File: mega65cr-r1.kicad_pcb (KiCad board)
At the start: 4 copper layers, 435 x 140 mm, 184 parts, among them J1 DB9_Male_MountingHoles, J10 Molex 46765-2301, J11 CON-SOCJ-2155, J12 Header for power lead to QMTE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, J13 Conn_01x04_Male, J14 Conn_02x17_Odd_Even, J15 696101000002 Fuse Holder 20mm, J16 Conn_01x04_Male, J17 C64_Tape_Port, J18 BA60BC0WT, J19 C64_User_Port, J2 DB9_Male_MountingHoles, J20 C64_Expansion_Port, J21 Audio Header, J22 DB15_Female_HighDensity_Mount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, J23 3.5mm_Stereo_Audio_Jack STX-3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, J24 Component A/V, J25 Joystick Ports Mezannine Lower, J26 Joystick Ports Mezannine Upper, J3 Wuerth_7499010121A, J4 QMTECH FPGA Module U4, J5 QMTECH FPGA Module U5, J6 SDF-60J for IEC 1541 serial p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, J7 QMTECH JTAG, J8 RTC, J9 1140084168 microSD Card Slot, P1 Full-side CD Card Slot, SW1 SW_Push_DPDT, U1 74LS373, U10 74LS06N, U11 74LS06N, U12 DP83826, U13 74LVC374, U14 PTN3363BSMP, U15 LM2678T-5.0, U16 74LVC374, U17 74LVC374, U18 74LS373, U19 74LS373, U2 74LVC374, U20 74LS125, U21 74LS125, U22 74LS06N, U23 74LVC374, U24 74LS125, U25 74LS373, U26 74LS373, U27 74LS138, U28 74LS138, U29 74LS137, U3 74LVC374, U30 74LS137, U31 74LS04, U32 74LVC374, U33 74LVC374, U34 74LVC374, U35 74LS373, U36 74LS373, U37 74LS373, U38 74LVC374, U39 74LVC374, U4 74LS373, U40 74LS373, U41 74LS373, U5 74LS06N, U6 74LVC374, U7 74LVC374, U8 74LS373, U9 74LS373

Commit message: replace remaining 74LS373 with 74LS374s #5
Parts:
- U1 (x2), U18, U19, U25, U26, U35, U36, U37, U4 (x2), U40, U41, U8, U9: value 74LS373 -> 74LS374

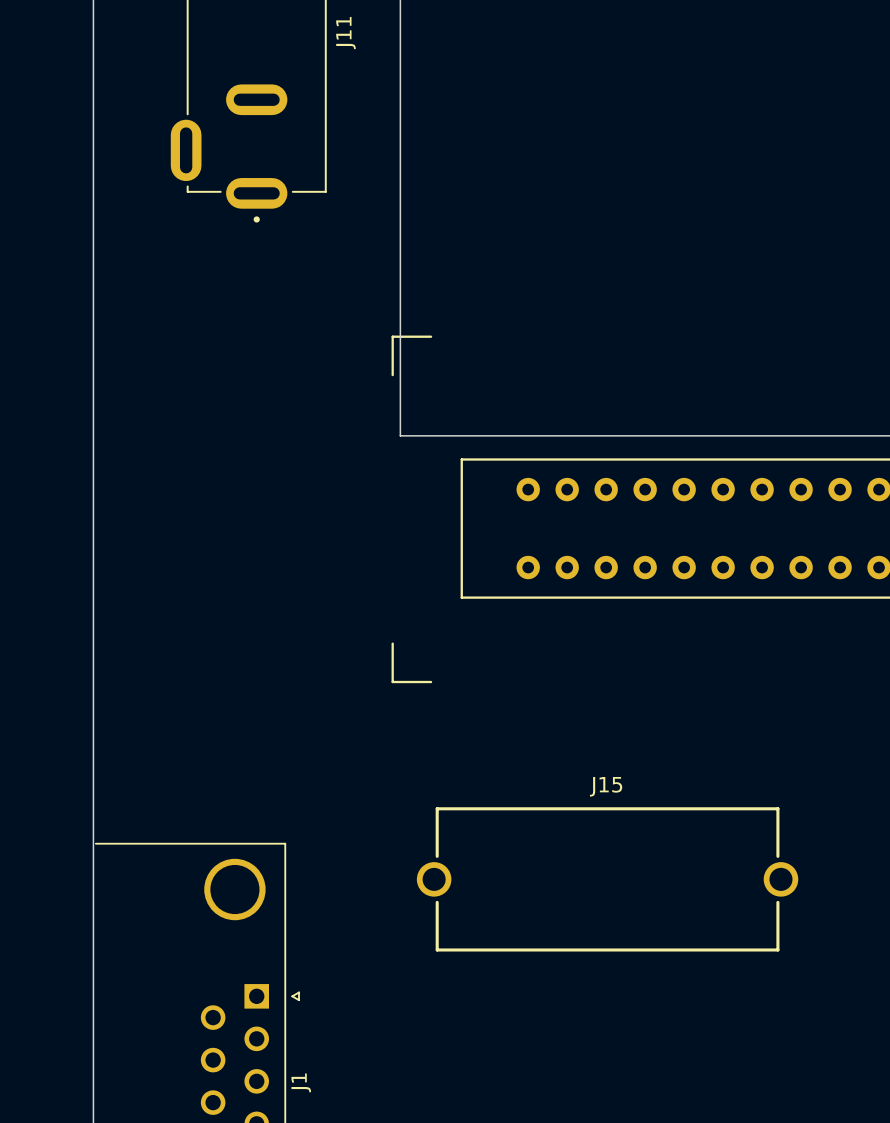
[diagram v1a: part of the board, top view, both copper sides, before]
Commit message: add missing power switch #7
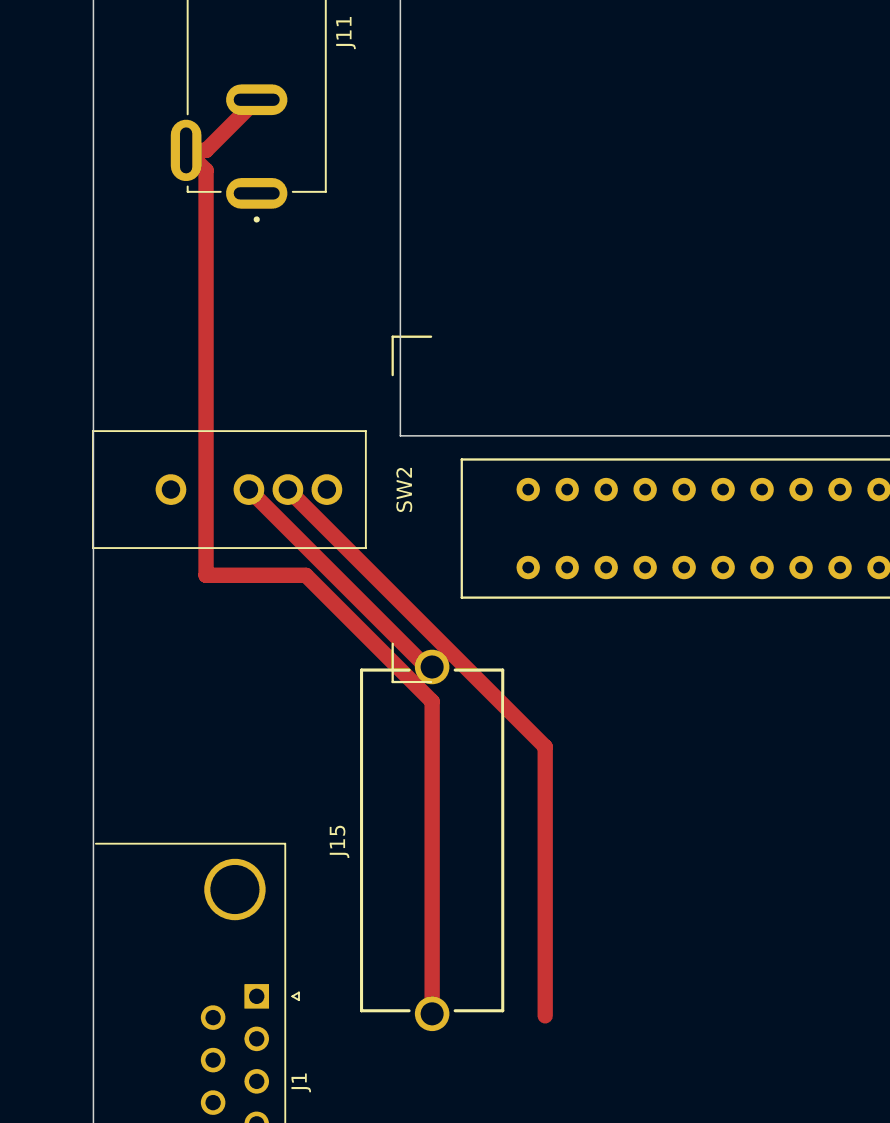
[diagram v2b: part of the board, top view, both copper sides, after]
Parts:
- added SW2: SW_SPDT_with_shield, snapeda:T103J1AVBE2, F.Cu at (50.3, 62.2)
- U1 (x2), U4 (x2), U9: value 74LS374 -> 74LS373
- moved J15 11.7 mm to (52.1, 86.4), turned to 90 degrees
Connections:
- J11 pad 2: /Power Supply/VBAT -> +12V_FUSED
- J11 pad 3: /Power Supply/VBAT -> +12V_FUSED
- J15 pad 1: /Power Supply/VBAT -> +12V_FUSED
- RN4 pad 4: /Cartridge Port/PHI2 -> unconnected-(RN4-Pad4)
- RN4 pad 5: /Cartridge Port/NMI_N -> /Cartridge Port/DMA_N
- RN4 pad 6: /Cartridge Port/RESET_N -> /Cartridge Port/R_W
- RN4 pad 7: /Cartridge Port/ROMH_N -> /Cartridge Port/NMI_N
- RN4 pad 8: /Cartridge Port/DMA_N -> /Cartridge Port/IRQ_N
- RN4 pad 9: /Cartridge Port/BA -> /Cartridge Port/RESET_N
- U32 pad 13: /Cartridge Port/NMI_N -> /Cartridge Port/DMA_N
- U32 pad 14: /Cartridge Port/PHI2 -> /Cartridge Port/ROML_N
- U32 pad 17: unconnected-(U32-Pad17) -> /Cartridge Port/ROMH_N
- U32 pad 18: unconnected-(U32-Pad18) -> /Cartridge Port/BA
- U32 pad 3: /Cartridge Port/BA -> /Cartridge Port/RESET_N
- U32 pad 4: /Cartridge Port/DMA_N -> /Cartridge Port/IRQ_N
- U32 pad 7: /Cartridge Port/ROMH_N -> /Cartridge Port/NMI_N
- U32 pad 8: /Cartridge Port/RESET_N -> /Cartridge Port/R_W
- U35 pad 12: /Cartridge Port/NMI_N -> /Cartridge Port/DMA_P_DRIVE
- U35 pad 15: /Cartridge Port/PHI2 -> /Cartridge Port/ROML_N
- U35 pad 16: unconnected-(U35-Pad16) -> /Cartridge Port/ROMH_N
- U35 pad 19: unconnected-(U35-Pad19) -> /Cartridge Port/BA
- U35 pad 2: /Cartridge Port/BA -> /Cartridge Port/RESET_P_DRIVE
- U35 pad 5: /Cartridge Port/DMA_N -> /Cartridge Port/IRQ_P_DRIVE
- U35 pad 6: /Cartridge Port/ROMH_N -> /Cartridge Port/NMI_P_DRIVE
- U35 pad 9: /Cartridge Port/RESET_N -> /Cartridge Port/W_R_DRIVE
- U38 pad 18: /Cartridge Port/ROML_N -> /Cartridge Port/PHI2
- U38 pad 3: /Cartridge Port/IRQ_N -> unconnected-(U38-Pad3)
- U38 pad 4: /Cartridge Port/R_W -> unconnected-(U38-Pad4)
- U40 pad 19: /Cartridge Port/ROML_N -> /Cartridge Port/PHI2
- U40 pad 2: /Cartridge Port/IRQ_N -> unconnected-(U40-Pad2)
- U40 pad 5: /Cartridge Port/R_W -> unconnected-(U40-Pad5)
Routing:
- net +12V_FUSED: track 0.00 -> 130.6 mm

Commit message: correct position of power input and switch and cart port
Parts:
- moved J11 3.44 mm to (37.2, 38.1)
- moved SW2 1.53 mm to (50.3, 63.8)
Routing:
- net +12V_FUSED: track 130.6 -> 132.1 mm
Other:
- outline, holes or cut-outs redrawn
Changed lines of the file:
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@@
   )
   (footprint "snapeda:GRAVITECH_CON-SOCJ-2155" (layer "F.Cu")
-    (at 40.64 38.1 -90)
+    (at 37.2 38.1 -90)
     (property "MANUFACTURER" "Gravitech")
     (property "MAXIMUM_PACKAGE_HEIGHT" "11.1 mm")
@@
   )
   (footprint "snapeda:T103J1AVBE2" (layer "F.Cu")
-    (at 50.292 62.23 90)
+    (at 50.292 63.76 90)
     (property "Sheetfile" "power.kicad_sch")
     (property "Sheetname" "Power Supply")
@@
   (gr_line (start 417.5 118.5) (end 439 140) (layer "Edge.Cuts") (width 0.1))
   (gr_line (start 360 65) (end 465 65) (layer "Edge.Cuts") (width 0.1))
-  (gr_line (start 120 30) (end 465 30) (layer "Edge.Cuts") (width 0.1))
+  (gr_line (start 121 30) (end 465 30) (layer "Edge.Cuts") (width 0.1))
   (gr_line (start 50 30) (end 50 60) (layer "Edge.Cuts") (width 0.1))
+  (gr_line (start 115 50) (end 115 60) (layer "Edge.Cuts") (width 0.1))
   (gr_line (start 360 170) (end 30 170) (layer "Edge.Cuts") (width 0.1))
   (gr_line (start 30 170) (end 30 30) (layer "Edge.Cuts") (width 0.1))
   (gr_line (start 360 170) (end 360 65) (layer "Edge.Cuts") (width 0.1))
   (gr_line (start 30 30) (end 50 30) (layer "Edge.Cuts") (width 0.1))
-  (gr_line (start 120 60) (end 120 30) (layer "Edge.Cuts") (width 0.1))
+  (gr_line (start 121 60) (end 115 60) (layer "Edge.Cuts") (width 0.1))
+  (gr_line (start 121 60) (end 121 30) (layer "Edge.Cuts") (width 0.1))
+  (gr_line (start 56 60) (end 56 50) (layer "Edge.Cuts") (width 0.1))
   (gr_line (start 465 30) (end 465 65) (layer "Edge.Cuts") (width 0.1))
   (gr_line (start 465 140) (end 465 65) (layer "Edge.Cuts") (width 0.1))
-  (gr_line (start 50 60) (end 120 60) (layer "Edge.Cuts") (width 0.1))
+  (gr_line (start 50 60) (end 56 60) (layer "Edge.Cuts") (width 0.1))
+  (gr_line (start 56 50) (end 115 50) (layer "Edge.Cuts") (width 0.1))
   (gr_text "MEGA65CR R1\nJoystick Port\nMezzannine" (at 439.367 126.716 270) (layer "F.SilkS")
     (effects (font (size 1 1) (thickness 0.15)) (justify left))
@@
   (segment (start 457.147 89.891) (end 457.65 89.891) (width 0.25) (layer "B.Cu") (net 2))
   (segment (start 453.347 80.991) (end 453.85 80.991) (width 0.25) (layer "B.Cu") (net 2))
-  (segment (start 37.338 42.698) (end 36.04 41.4) (width 1) (layer "F.Cu") (net 3))
+  (segment (start 37.338 69.088) (end 37.338 51.562) (width 1) (layer "F.Cu") (net 3))
+  (segment (start 52.07 97.66) (end 52.07 77.311143) (width 1) (layer "F.Cu") (net 3))
   (segment (start 59.436 80.264) (end 59.436 97.79) (width 1) (layer "F.Cu") (net 3))
-  (segment (start 37.338 69.088) (end 37.338 42.698) (width 1) (layer "F.Cu") (net 3))
-  (segment (start 36.04 41.4) (end 37.34 41.4) (width 1) (layer "F.Cu") (net 3))
+  (segment (start 37.338 51.562) (end 32.6 46.824) (width 1) (layer "F.Cu") (net 3))
   (segment (start 43.846857 69.088) (end 37.338 69.088) (width 1) (layer "F.Cu") (net 3))
+  (segment (start 32.6 41.4) (end 33.9 41.4) (width 1) (layer "F.Cu") (net 3))
   (segment (start 40.132 63.5) (end 51.692 75.06) (width 1) (layer "F.Cu") (net 3))
+  (segment (start 33.9 41.4) (end 37.2 38.1) (width 1) (layer "F.Cu") (net 3))
+  (segment (start 32.6 46.824) (end 32.6 41.4) (width 1) (layer "F.Cu") (net 3))
   (segment (start 42.672 63.5) (end 59.436 80.264) (width 1) (layer "F.Cu") (net 3))
-  (segment (start 52.07 97.66) (end 52.07 77.311143) (width 1) (layer "F.Cu") (net 3))
   (segment (start 52.07 77.311143) (end 43.846857 69.088) (width 1) (layer "F.Cu") (net 3))
-  (segment (start 37.34 41.4) (end 40.64 38.1) (width 1) (layer "F.Cu") (net 3))
   (segment (start 51.692 75.06) (end 52.07 75.06) (width 0.25) (layer "B.Cu") (net 3))
   (segment (start 457.782 85.446) (end 457.782 82.774) (width 0.25) (layer "B.Cu") (net 6))

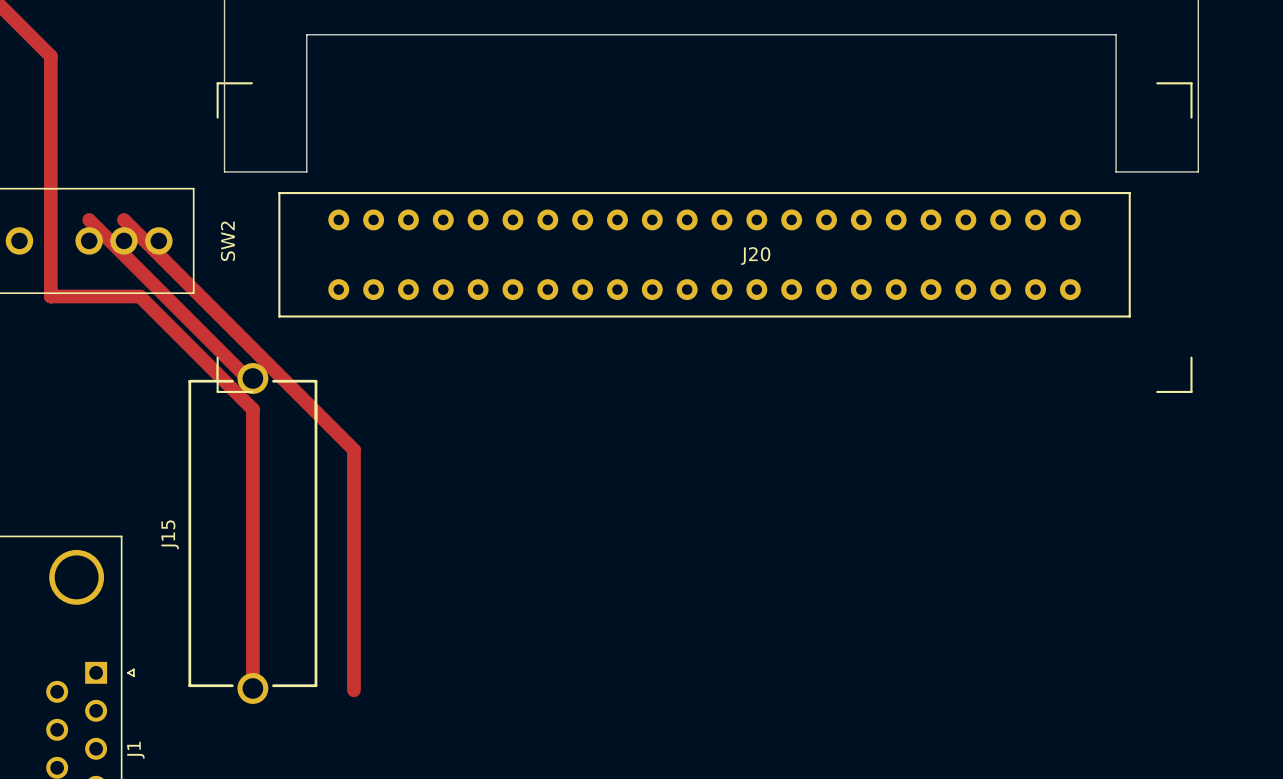
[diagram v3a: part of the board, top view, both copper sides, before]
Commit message: further fix cart port and power switch connections #2
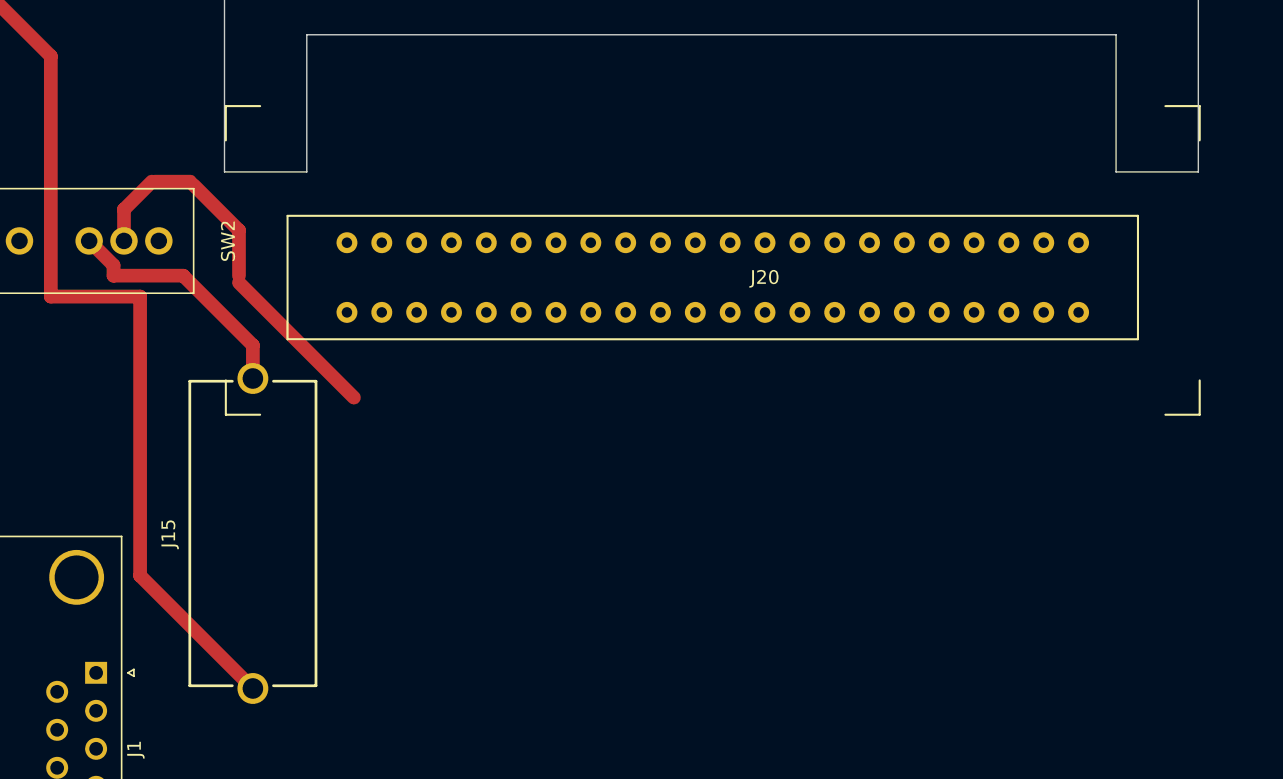
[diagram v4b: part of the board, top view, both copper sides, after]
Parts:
- moved J20 1.76 mm to (85.6, 67.7)
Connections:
- J11 pad 2: +12V_FUSED -> Net-(SW2-Pad3)
- J11 pad 3: +12V_FUSED -> Net-(SW2-Pad3)
- J15 pad 1: +12V_FUSED -> Net-(SW2-Pad3)
- J15 pad 2: +12V_FUSED -> Net-(SW2-Pad3)
- SW2 pad 3: +12V_FUSED -> Net-(SW2-Pad3)
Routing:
- net +12V_FUSED: track 132.1 -> 28.7 mm
- net Net-(SW2-Pad3): track 0.00 -> 92.4 mm
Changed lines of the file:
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@@
   (net 502 "unconnected-(U40-Pad5)")
   (net 503 "unconnected-(SW2-Pad1)")
+  (net 504 "Net-(SW2-Pad3)")
   (footprint "Resistor_THT:R_Axial_DIN0204_L3.6mm_D1.6mm_P7.62mm_Horizontal" (layer "F.Cu")
     (at 183.61 287.04)
@@
       (net 180 "unconnected-(J11-Pad1)") (pintype "passive"))
     (pad "2" thru_hole oval locked (at 3.3 4.6 270) (size 4 2) (drill oval 3 0.8) (layers *.Cu *.Mask)
-      (net 3 "+12V_FUSED") (pintype "passive"))
+      (net 504 "Net-(SW2-Pad3)") (pintype "passive"))
     (pad "3" thru_hole oval locked (at 0 0 270) (size 2 4) (drill oval 0.8 3) (layers *.Cu *.Mask)
-      (net 3 "+12V_FUSED") (pintype "passive"))
+      (net 504 "Net-(SW2-Pad3)") (pintype "passive"))
   )
   (footprint "Resistor_THT:R_Box_L8.4mm_W2.5mm_P5.08mm" (layer "F.Cu")
@@
   )
   (footprint "HackupNet:C64-Cart-Socket-Vertical" (layer "F.Cu")
-    (at 85 66.04)
+    (at 85.598 67.7)
     (property "Sheetfile" "expansionport.kicad_sch")
     (property "Sheetname" "Cartridge Port")
@@
     (fp_line (start 11 -4.5) (end 11 4.5) (layer "F.Fab") (width 0.1))
     (pad "1" thru_hole circle locked (at -11.3 0 90) (size 2.25 2.25) (drill 1.5) (layers *.Cu *.Mask)
-      (net 3 "+12V_FUSED") (pintype "passive"))
+      (net 504 "Net-(SW2-Pad3)") (pintype "passive"))
     (pad "2" thru_hole circle locked (at 11.3 0 90) (size 2.25 2.25) (drill 1.5) (layers *.Cu *.Mask)
-      (net 3 "+12V_FUSED") (pintype "passive"))
+      (net 504 "Net-(SW2-Pad3)") (pintype "passive"))
   )
   (footprint "Package_DIP:DIP-20_W7.62mm" (layer "F.Cu")
@@
       (net 3 "+12V_FUSED") (pinfunction "B") (pintype "passive"))
     (pad "3" thru_hole circle (at -1.27 -10.16 90) (size 2 2) (drill 1.2) (layers *.Cu *.Mask)
-      (net 3 "+12V_FUSED") (pinfunction "C") (pintype "passive"))
+      (net 504 "Net-(SW2-Pad3)") (pinfunction "C") (pintype "passive"))
     (pad "SH" thru_hole circle (at -1.27 -15.24 90) (size 2 2) (drill 1.2) (layers *.Cu *.Mask)
       (net 2 "GND") (pinfunction "SHIELD") (pintype "passive"))
@@
   (segment (start 457.147 89.891) (end 457.65 89.891) (width 0.25) (layer "B.Cu") (net 2))
   (segment (start 453.347 80.991) (end 453.85 80.991) (width 0.25) (layer "B.Cu") (net 2))
-  (segment (start 37.338 69.088) (end 37.338 51.562) (width 1) (layer "F.Cu") (net 3))
-  (segment (start 52.07 97.66) (end 52.07 77.311143) (width 1) (layer "F.Cu") (net 3))
-  (segment (start 59.436 80.264) (end 59.436 97.79) (width 1) (layer "F.Cu") (net 3))
-  (segment (start 37.338 51.562) (end 32.6 46.824) (width 1) (layer "F.Cu") (net 3))
-  (segment (start 43.846857 69.088) (end 37.338 69.088) (width 1) (layer "F.Cu") (net 3))
-  (segment (start 32.6 41.4) (end 33.9 41.4) (width 1) (layer "F.Cu") (net 3))
-  (segment (start 40.132 63.5) (end 51.692 75.06) (width 1) (layer "F.Cu") (net 3))
-  (segment (start 33.9 41.4) (end 37.2 38.1) (width 1) (layer "F.Cu") (net 3))
-  (segment (start 32.6 46.824) (end 32.6 41.4) (width 1) (layer "F.Cu") (net 3))
-  (segment (start 42.672 63.5) (end 59.436 80.264) (width 1) (layer "F.Cu") (net 3))
-  (segment (start 52.07 77.311143) (end 43.846857 69.088) (width 1) (layer "F.Cu") (net 3))
-  (segment (start 51.692 75.06) (end 52.07 75.06) (width 0.25) (layer "B.Cu") (net 3))
+  (segment (start 42.672 62.738) (end 44.704 60.706) (width 1) (layer "F.Cu") (net 3))
+  (segment (start 51.054 64.262) (end 51.054 67.564) (width 1) (layer "F.Cu") (net 3))
+  (segment (start 51.054 68.072) (end 59.436 76.454) (width 1) (layer "F.Cu") (net 3))
+  (segment (start 51.054 67.564) (end 51.054 68.072) (width 0.25) (layer "F.Cu") (net 3))
+  (segment (start 42.672 65.03) (end 42.672 62.738) (width 1) (layer "F.Cu") (net 3))
+  (segment (start 44.958 60.706) (end 47.498 60.706) (width 1) (layer "F.Cu") (net 3))
+  (segment (start 47.752 60.96) (end 51.054 64.262) (width 1) (layer "F.Cu") (net 3))
+  (segment (start 47.498 60.706) (end 47.752 60.96) (width 0.25) (layer "F.Cu") (net 3))
+  (segment (start 44.704 60.706) (end 44.958 60.706) (width 0.25) (layer "F.Cu") (net 3))
   (segment (start 457.782 85.446) (end 457.782 82.774) (width 0.25) (layer "B.Cu") (net 6))
   (segment (start 442.851031 67.351969) (end 442.851031 66.716969) (width 0.25) (layer "B.Cu") (net 6))
@@
   (segment (start 440.368794 136.735511) (end 423.364641 119.731359) (width 0.25) (layer "B.Cu") (net 491))
   (segment (start 449.50565 136.34665) (end 449.116789 136.735511) (width 0.25) (layer "B.Cu") (net 491))
+  (segment (start 37.338 69.088) (end 37.338 51.562) (width 1) (layer "F.Cu") (net 504))
+  (segment (start 43.846857 69.088) (end 43.846857 89.436857) (width 1) (layer "F.Cu") (net 504))
+  (segment (start 41.91 67.564) (end 46.99 67.564) (width 1) (layer "F.Cu") (net 504))
+  (segment (start 37.338 51.562) (end 32.6 46.824) (width 1) (layer "F.Cu") (net 504))
+  (segment (start 43.846857 69.088) (end 37.338 69.088) (width 1) (layer "F.Cu") (net 504))
+  (segment (start 32.6 41.4) (end 33.9 41.4) (width 1) (layer "F.Cu") (net 504))
+  (segment (start 33.9 41.4) (end 37.2 38.1) (width 1) (layer "F.Cu") (net 504))
+  (segment (start 41.91 66.808) (end 41.91 67.564) (width 1) (layer "F.Cu") (net 504))
+  (segment (start 52.07 72.644) (end 52.07 75.06) (width 1) (layer "F.Cu") (net 504))
+  (segment (start 32.6 46.824) (end 32.6 41.4) (width 1) (layer "F.Cu") (net 504))
+  (segment (start 46.99 67.564) (end 52.07 72.644) (width 1) (layer "F.Cu") (net 504))
+  (segment (start 40.132 65.03) (end 41.91 66.808) (width 1) (layer "F.Cu") (net 504))
+  (segment (start 43.846857 89.436857) (end 52.07 97.66) (width 1) (layer "F.Cu") (net 504))
+  (segment (start 51.692 75.06) (end 52.07 75.06) (width 0.25) (layer "B.Cu") (net 504))
   (zone (net 2) (net_name "GND") (layers "In1.Cu" "In2.Cu") (hatch edge 0.508)
     (connect_pads (clearance 0.508))

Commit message: correct port positions and cutouts #2
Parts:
- moved J23 11.5 mm to (240.0, 38.1)
- moved J9 10.3 mm to (226.0, 41.0)
- moved J10 8.94 mm to (189.0, 41.0)
- moved J22 8.63 mm to (157.0, 43.0)
- moved U14 7.48 mm to (193.4, 53.2)
- moved J24 6.56 mm to (352.0, 38.1)
- moved J3 5.95 mm to (205.5, 45.6)
- moved J17 4.53 mm to (442.0, 41.3)
- moved U10 1.48 mm to (445.7, 92.6)
- moved U5 1.48 mm to (445.7, 69.8)
- moved J26 1.48 mm to (457.1, 88.8)
- moved U11 1.48 mm to (421.6, 100.2)
- moved U6 1.48 mm to (434.3, 69.8)
- moved U7 1.48 mm to (421.6, 69.7)
- moved U8 1.48 mm to (445.7, 114.2)
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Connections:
- J11 pad 2: Net-(SW2-Pad3) -> /Power Supply/VBAT
- J11 pad 3: Net-(SW2-Pad3) -> /Power Supply/VBAT
- J15 pad 1: Net-(SW2-Pad3) -> /Power Supply/VBAT
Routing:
- net Net-(SW2-Pad3): track 92.4 -> 18.3 mm
- net /Power Supply/VBAT: track 0.00 -> 74.1 mm
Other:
- board size 435 x 140 mm -> 435 x 140.6 mm
